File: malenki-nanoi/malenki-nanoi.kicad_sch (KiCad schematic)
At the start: 23 parts, among them J1 Conn_01x02_Male, J2 Conn_01x03, J3 Conn_01x02, J5 Conn_01x02_Male, J6 Conn_01x02_Male, J7 Conn_01x02_Male, U2 AIC1734-33GUTR, U3 ATtiny1616-M, U5 DRV8837DSGR, U6 DRV8837DSGR, U7 DRV8837DSGR

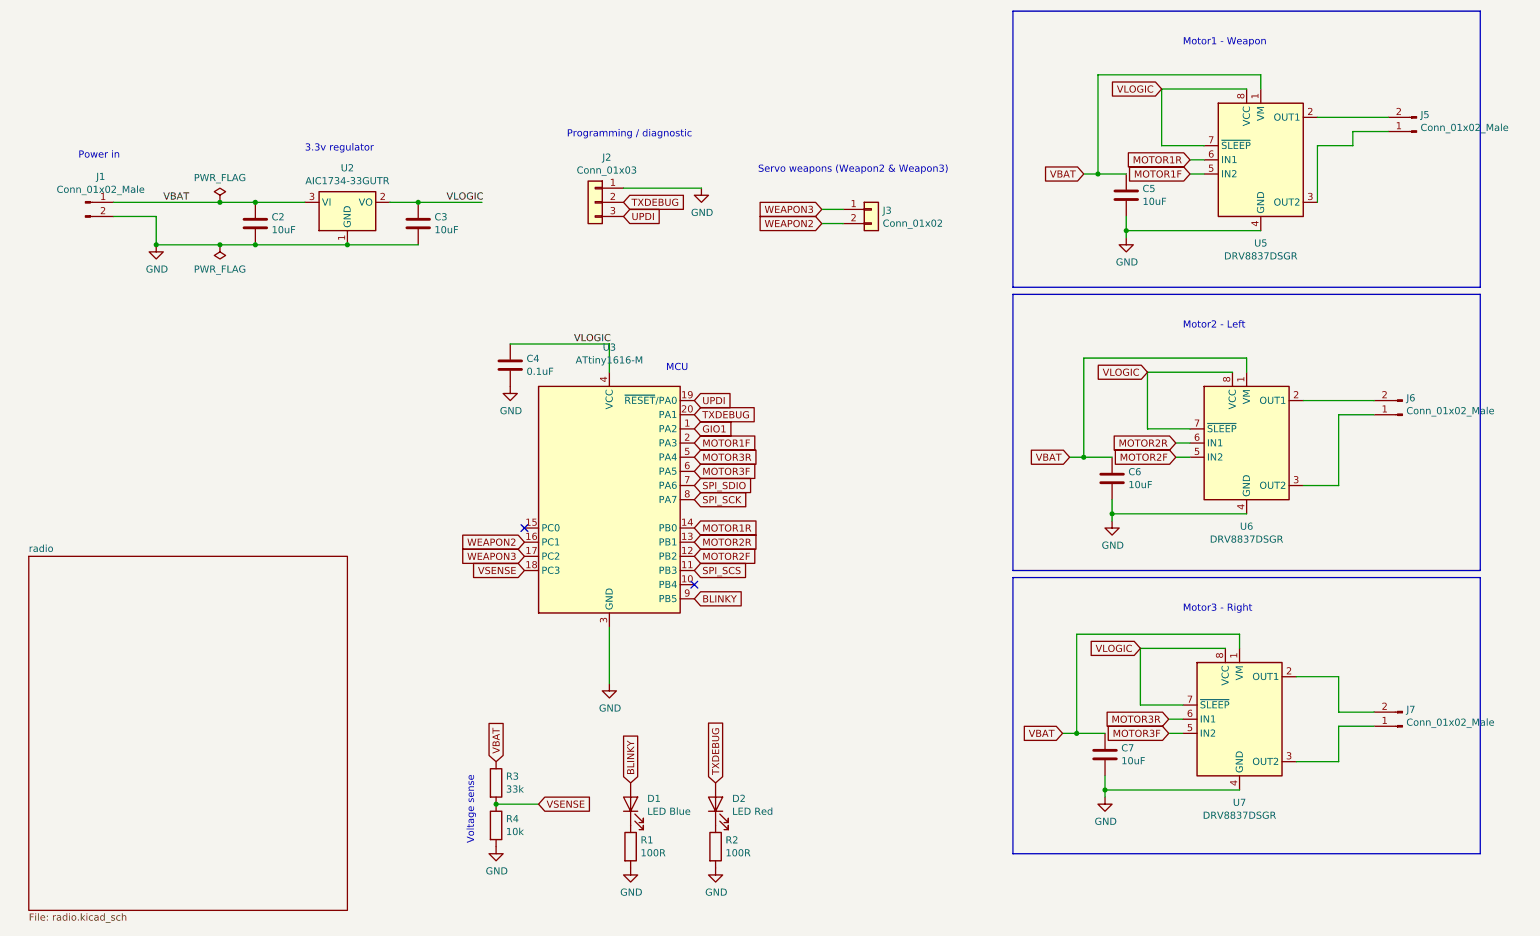
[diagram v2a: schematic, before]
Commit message: 4-layer Malenki-nano
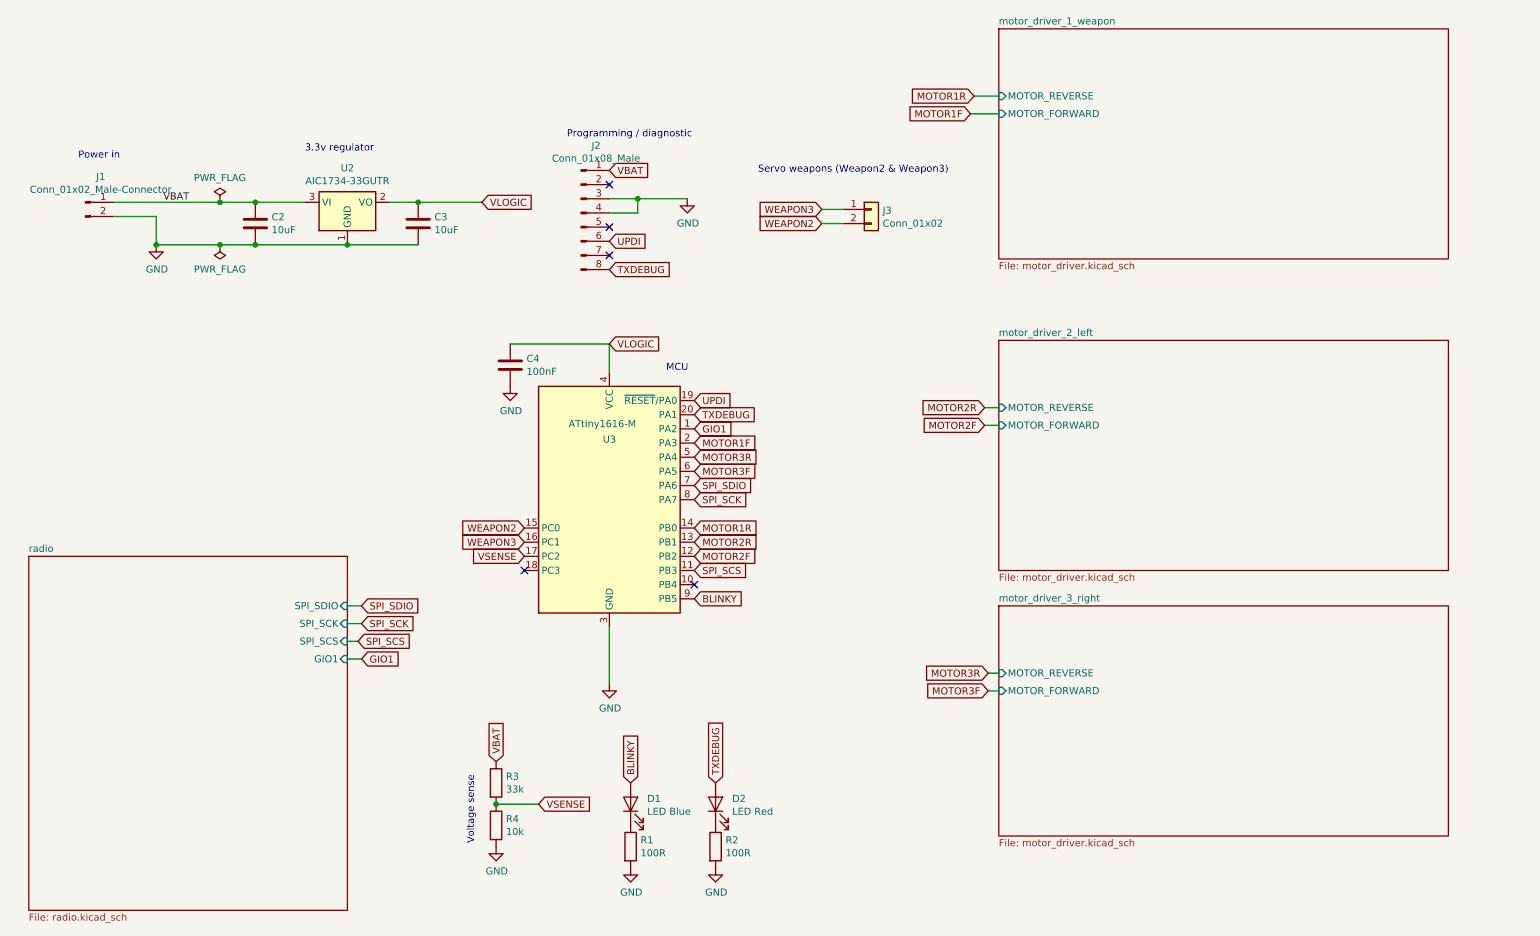
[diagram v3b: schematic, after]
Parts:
- removed C5, C6, C7: 10uF, Capacitor_SMD:C_0603_1608Metric, symbol malenki-nano-rescue:C-Device
- removed J2: Conn_01x03, Connector_PinHeader_2.00mm:PinHeader_1x03_P2.00mm_Vertical, symbol Connector_Generic:Conn_01x03
- removed J5, J6, J7: Conn_01x02_Male, malenki-nano:PinHeader_1x02_P2.54mm_BIG1, symbol malenki-nano-rescue:Conn_01x02_Male-Connector
- removed U5, U6, U7: DRV8837DSGR, malenki-nano:WSON-8-1EP_2x2mm_P0.5mm_HAND1, symbol Driver_Motor:DRV8837C
- added J2: Conn_01x08_Male, malenki-nano:SOIC_clipProgSmall, symbol Connector:Conn_01x08_Male
- C2, C3: LCSC C19702 -> (none)
- C4: value 0.1uF -> 100nF; footprint Capacitor_SMD:C_0603_1608Metric -> Capacitor_SMD:C_0402_1005Metric; LCSC C14663 -> (none)
- D1, D2: footprint LED_SMD:LED_0603_1608Metric_Castellated -> LED_SMD:LED_0603_1608Metric
- J1: value Conn_01x02_Male -> Conn_01x02_Male-Connector
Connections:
- net GND: now also J2.3 (Pin_3), J2.4 (Pin_4)
- net TXDEBUG: now also J2.8 (Pin_8)
- net UPDI: now also J2.6 (Pin_6)
- net VBAT: now also J2.1 (Pin_1)
- net VSENSE: now also U3.17 (PC2); no longer U3.18 (PC3)
- net WEAPON2: now also U3.15 (PC0); no longer U3.16 (PC1)
- net WEAPON3: now also U3.16 (PC1); no longer U3.17 (PC2)
- no-connect marks 2 -> 5
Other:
- added sheet motor_driver_1_weapon (motor_driver.kicad_sch)
- added sheet motor_driver_2_left (motor_driver.kicad_sch)
- added sheet motor_driver_3_right (motor_driver.kicad_sch)
- sheet radio ports: added GIO1, SPI_SCK, SPI_SCS, SPI_SDIO; removed none
- note removed: "Motor1 - Weapon"
- note removed: "Motor2 - Left"
- note removed: "Motor3 - Right"

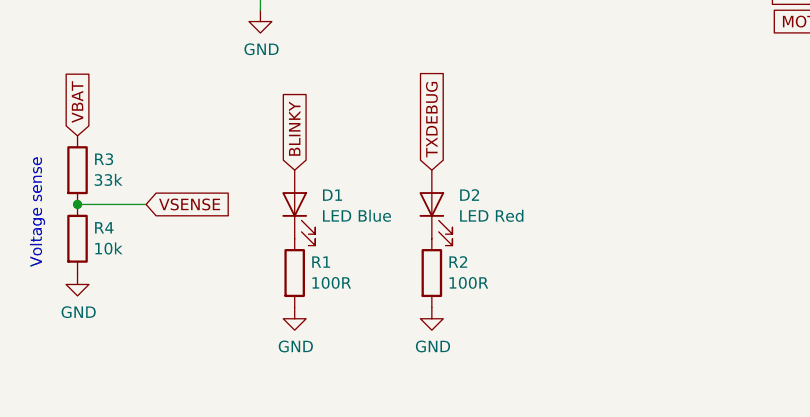
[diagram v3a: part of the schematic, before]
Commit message: Crystal caps update
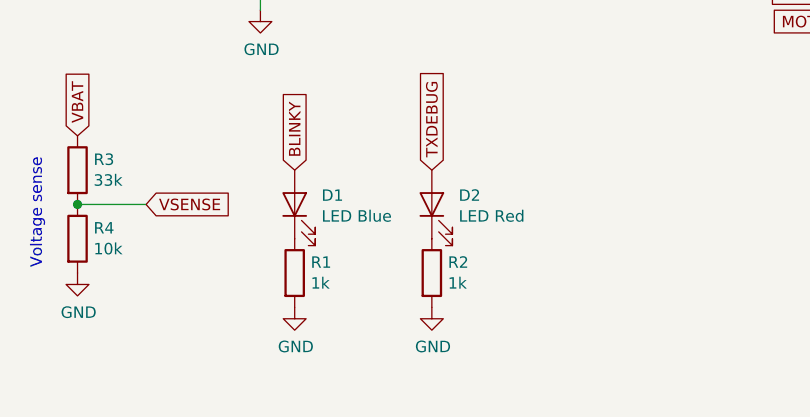
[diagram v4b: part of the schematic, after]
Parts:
- R1, R2: value 100R -> 1k; LCSC C22775 -> (none)
- R3: LCSC C4216 -> (none)
- R4: LCSC C25804 -> (none)
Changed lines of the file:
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@@
   (junction (at 106.68 156.21) (diameter 1.016) (color 0 0 0 0))
   (junction (at 132.08 47.625) (diameter 1.016) (color 0 0 0 0))
+  (no_connect (at 127 57.785))
+  (no_connect (at 142.24 116.84))
+  (no_connect (at 127 52.705))
+  (no_connect (at 111.76 114.3))
   (no_connect (at 127 45.085))
-  (no_connect (at 111.76 114.3))
-  (no_connect (at 142.24 116.84))
-  (no_connect (at 127 57.785))
-  (no_connect (at 127 52.705))
   (wire (pts (xy 38.1 48.26) (xy 57.15 48.26))
     (stroke (width 0) (type solid) (color 0 0 0 0))
@@
       (effects (font (size 1.27 1.27)) hide)
     )
-    (property "LCSC" "C4216" (id 5) (at 106.68 152.4 0)
+    (property "LCSC" "" (id 5) (at 106.68 152.4 0)
       (effects (font (size 1.27 1.27)) hide)
     )
@@
       (effects (font (size 1.27 1.27)) hide)
     )
-    (property "LCSC" "C25804" (id 5) (at 106.68 160.02 0)
+    (property "LCSC" "" (id 5) (at 106.68 160.02 0)
       (effects (font (size 1.27 1.27)) hide)
     )
@@
       (effects (font (size 1.27 1.27)) (justify left))
     )
-    (property "Value" "100R" (id 1) (at 132.588 164.973 0)
+    (property "Value" "1k" (id 1) (at 132.588 164.973 0)
       (effects (font (size 1.27 1.27)) (justify left))
     )
@@
       (effects (font (size 1.27 1.27)) hide)
     )
-    (property "LCSC" "C22775" (id 5) (at 130.81 163.83 0)
+    (property "LCSC" "" (id 5) (at 130.81 163.83 0)
       (effects (font (size 1.27 1.27)) hide)
     )
@@
       (effects (font (size 1.27 1.27)) (justify left))
     )
-    (property "Value" "100R" (id 1) (at 147.828 164.973 0)
+    (property "Value" "1k" (id 1) (at 147.828 164.973 0)
       (effects (font (size 1.27 1.27)) (justify left))
     )
@@
       (effects (font (size 1.27 1.27)) hide)
     )
-    (property "LCSC" "C22775" (id 5) (at 146.05 163.83 0)
+    (property "LCSC" "" (id 5) (at 146.05 163.83 0)
       (effects (font (size 1.27 1.27)) hide)
     )
@@
     )
     (path "/f11a69ac-2dce-40ba-8e3e-2f36b56ed9c7"
-      (reference "R1") (unit 1) (value "100R") (footprint "Resistor_SMD:R_0603_1608Metric")
+      (reference "R1") (unit 1) (value "1k") (footprint "Resistor_SMD:R_0603_1608Metric")
     )
     (path "/29ed0b48-8134-4efe-ba29-799f5df4563b"
-      (reference "R2") (unit 1) (value "100R") (footprint "Resistor_SMD:R_0603_1608Metric")
+      (reference "R2") (unit 1) (value "1k") (footprint "Resistor_SMD:R_0603_1608Metric")
     )
     (path "/9f9c8013-6ba2-4b1f-817e-7aeb8f9ad091"
@@
     )
     (path "/f8865f8d-c9c7-4324-8715-db444b940a42/215e83d2-e873-4735-b43d-b93e560e3c41"
-      (reference "C14") (unit 1) (value "33pF") (footprint "Capacitor_SMD:C_0402_1005Metric")
+      (reference "C14") (unit 1) (value "22pF") (footprint "Capacitor_SMD:C_0402_1005Metric")
     )
     (path "/f8865f8d-c9c7-4324-8715-db444b940a42/089b699b-7234-4ca1-8596-c8152df860db"
-      (reference "C15") (unit 1) (value "33pF") (footprint "Capacitor_SMD:C_0402_1005Metric")
+      (reference "C15") (unit 1) (value "22pF") (footprint "Capacitor_SMD:C_0402_1005Metric")
     )
     (path "/f8865f8d-c9c7-4324-8715-db444b940a42/d104f9b6-35d9-40fd-8206-1975fac53040"

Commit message: Use hand-solder footprints for all 0402
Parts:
- C4: footprint Capacitor_SMD:C_0402_1005Metric -> Capacitor_SMD:C_0402_1005Metric_Pad0.74x0.62mm_HandSolder
- J1, J2: now left out of the parts list
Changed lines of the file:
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@@
   (junction (at 106.68 156.21) (diameter 1.016) (color 0 0 0 0))
   (junction (at 132.08 47.625) (diameter 1.016) (color 0 0 0 0))
+  (no_connect (at 111.76 114.3))
+  (no_connect (at 127 52.705))
   (no_connect (at 127 57.785))
+  (no_connect (at 127 45.085))
   (no_connect (at 142.24 116.84))
-  (no_connect (at 127 52.705))
-  (no_connect (at 111.76 114.3))
-  (no_connect (at 127 45.085))
   (wire (pts (xy 38.1 48.26) (xy 57.15 48.26))
     (stroke (width 0) (type solid) (color 0 0 0 0))
@@
   )
   (symbol (lib_id "malenki-nano-rescue:Conn_01x02_Male-Connector") (at 33.02 48.26 0) (unit 1)
-    (in_bom yes) (on_board yes)
+    (in_bom no) (on_board yes)
     (property "Reference" "J1" (id 0) (at 35.7632 43.6626 0))
     (property "Value" "Conn_01x02_Male-Connector" (id 1) (at 35.7632 45.974 0))
@@
       (effects (font (size 1.27 1.27)) (justify left))
     )
-    (property "Footprint" "Capacitor_SMD:C_0402_1005Metric" (id 2) (at 110.1852 81.28 0)
+    (property "Footprint" "Capacitor_SMD:C_0402_1005Metric_Pad0.74x0.62mm_HandSolder" (id 2) (at 110.1852 81.28 0)
       (effects (font (size 1.27 1.27)) hide)
     )
@@
   )
   (symbol (lib_id "Connector:Conn_01x08_Male") (at 121.92 50.165 0) (unit 1)
-    (in_bom yes) (on_board yes)
+    (in_bom no) (on_board yes)
     (property "Reference" "J2" (id 0) (at 124.6124 38.0808 0))
     (property "Value" "Conn_01x08_Male" (id 1) (at 124.6124 40.3795 0))
@@
     )
     (path "/743e3bfd-2846-452f-87cb-c439c582f82c"
-      (reference "C4") (unit 1) (value "100nF") (footprint "Capacitor_SMD:C_0402_1005Metric")
+      (reference "C4") (unit 1) (value "100nF") (footprint "Capacitor_SMD:C_0402_1005Metric_Pad0.74x0.62mm_HandSolder")
     )
     (path "/873f0869-df80-4fe6-817c-973a36517086"
@@
     )
     (path "/f8865f8d-c9c7-4324-8715-db444b940a42/66cb42e5-4d9e-40a2-a2c4-9364eaae7141"
-      (reference "C9") (unit 1) (value "1pF") (footprint "Capacitor_SMD:C_0402_1005Metric")
+      (reference "C9") (unit 1) (value "1pF") (footprint "Capacitor_SMD:C_0402_1005Metric_Pad0.74x0.62mm_HandSolder")
     )
     (path "/f8865f8d-c9c7-4324-8715-db444b940a42/19f9ce3e-6112-47c3-be9c-52edb46d1400"
-      (reference "C10") (unit 1) (value "22pF") (footprint "Capacitor_SMD:C_0402_1005Metric")
+      (reference "C10") (unit 1) (value "22pF") (footprint "Capacitor_SMD:C_0402_1005Metric_Pad0.74x0.62mm_HandSolder")
     )
     (path "/f8865f8d-c9c7-4324-8715-db444b940a42/19c72677-c166-4d54-8f59-572a153580c0"
-      (reference "C11") (unit 1) (value "10pF") (footprint "Capacitor_SMD:C_0402_1005Metric")
+      (reference "C11") (unit 1) (value "10pF") (footprint "Capacitor_SMD:C_0402_1005Metric_Pad0.74x0.62mm_HandSolder")
     )
     (path "/f8865f8d-c9c7-4324-8715-db444b940a42/0b0030e3-97d6-4726-b917-72c61fef63d8"
-      (reference "C12") (unit 1) (value "100nF") (footprint "Capacitor_SMD:C_0402_1005Metric")
+      (reference "C12") (unit 1) (value "100nF") (footprint "Capacitor_SMD:C_0402_1005Metric_Pad0.74x0.62mm_HandSolder")
     )
     (path "/f8865f8d-c9c7-4324-8715-db444b940a42/f33e7671-b9c8-40c2-9120-c03d59cd8f50"
-      (reference "C13") (unit 1) (value "100nF") (footprint "Capacitor_SMD:C_0402_1005Metric")
+      (reference "C13") (unit 1) (value "100nF") (footprint "Capacitor_SMD:C_0402_1005Metric_Pad0.74x0.62mm_HandSolder")
     )
     (path "/f8865f8d-c9c7-4324-8715-db444b940a42/215e83d2-e873-4735-b43d-b93e560e3c41"
-      (reference "C14") (unit 1) (value "22pF") (footprint "Capacitor_SMD:C_0402_1005Metric")
+      (reference "C14") (unit 1) (value "22pF") (footprint "Capacitor_SMD:C_0402_1005Metric_Pad0.74x0.62mm_HandSolder")
     )
     (path "/f8865f8d-c9c7-4324-8715-db444b940a42/089b699b-7234-4ca1-8596-c8152df860db"
-      (reference "C15") (unit 1) (value "22pF") (footprint "Capacitor_SMD:C_0402_1005Metric")
+      (reference "C15") (unit 1) (value "22pF") (footprint "Capacitor_SMD:C_0402_1005Metric_Pad0.74x0.62mm_HandSolder")
     )
     (path "/f8865f8d-c9c7-4324-8715-db444b940a42/d104f9b6-35d9-40fd-8206-1975fac53040"
-      (reference "C16") (unit 1) (value "100nF") (footprint "Capacitor_SMD:C_0402_1005Metric")
+      (reference "C16") (unit 1) (value "100nF") (footprint "Capacitor_SMD:C_0402_1005Metric_Pad0.74x0.62mm_HandSolder")
     )
     (path "/f8865f8d-c9c7-4324-8715-db444b940a42/ed3b10e6-1f62-4694-a165-a81089d52184"
-      (reference "C17") (unit 1) (value "100nF") (footprint "Capacitor_SMD:C_0402_1005Metric")
+      (reference "C17") (unit 1) (value "100nF") (footprint "Capacitor_SMD:C_0402_1005Metric_Pad0.74x0.62mm_HandSolder")
     )
     (path "/f8865f8d-c9c7-4324-8715-db444b940a42/dfcc0291-fde2-4968-8dfe-dc0fed520275"
-      (reference "C18") (unit 1) (value "560pF") (footprint "Capacitor_SMD:C_0402_1005Metric")
+      (reference "C18") (unit 1) (value "560pF") (footprint "Capacitor_SMD:C_0402_1005Metric_Pad0.74x0.62mm_HandSolder")
     )
     (path "/f8865f8d-c9c7-4324-8715-db444b940a42/61da5400-349c-4f48-a162-f52487e1921d"
-      (reference "C19") (unit 1) (value "10nF") (footprint "Capacitor_SMD:C_0402_1005Metric")
+      (reference "C19") (unit 1) (value "10nF") (footprint "Capacitor_SMD:C_0402_1005Metric_Pad0.74x0.62mm_HandSolder")
     )
     (path "/f8865f8d-c9c7-4324-8715-db444b940a42/6545753d-6d1e-4127-b61a-3db1ceec6d42"
@@
     )
     (path "/f8865f8d-c9c7-4324-8715-db444b940a42/52e761a0-c28e-41e0-a3bd-b32a8696a976"
-      (reference "C22") (unit 1) (value "100nF") (footprint "Capacitor_SMD:C_0402_1005Metric")
+      (reference "C22") (unit 1) (value "100nF") (footprint "Capacitor_SMD:C_0402_1005Metric_Pad0.74x0.62mm_HandSolder")
     )
     (path "/f8865f8d-c9c7-4324-8715-db444b940a42/f65ffae7-fc80-4563-89b6-6365862c5faa"
-      (reference "C23") (unit 1) (value "100nF") (footprint "Capacitor_SMD:C_0402_1005Metric")
+      (reference "C23") (unit 1) (value "100nF") (footprint "Capacitor_SMD:C_0402_1005Metric_Pad0.74x0.62mm_HandSolder")
     )
     (path "/f8865f8d-c9c7-4324-8715-db444b940a42/d45315c2-46f0-47a6-b716-e74dc67406db"
-      (reference "L1") (unit 1) (value "2.7nH") (footprint "Inductor_SMD:L_0402_1005Metric")
+      (reference "L1") (unit 1) (value "2.7nH") (footprint "Inductor_SMD:L_0402_1005Metric_Pad0.77x0.64mm_HandSolder")
     )
     (path "/f8865f8d-c9c7-4324-8715-db444b940a42/580c6d2b-a8e3-498e-8012-27d587656f3b"
-      (reference "L2") (unit 1) (value "4.7nH") (footprint "Inductor_SMD:L_0402_1005Metric")
+      (reference "L2") (unit 1) (value "4.7nH") (footprint "Inductor_SMD:L_0402_1005Metric_Pad0.77x0.64mm_HandSolder")
     )
     (path "/f8865f8d-c9c7-4324-8715-db444b940a42/c420d0bf-bb38-4822-8699-2971a00ad3de"
-      (reference "L3") (unit 1) (value "4.7nH") (footprint "Inductor_SMD:L_0402_1005Metric")
+      (reference "L3") (unit 1) (value "4.7nH") (footprint "Inductor_SMD:L_0402_1005Metric_Pad0.77x0.64mm_HandSolder")
     )
     (path "/f8865f8d-c9c7-4324-8715-db444b940a42/5902e9a6-0dad-47d3-b107-e5e2b73c9336"
-      (reference "R5") (unit 1) (value "200R") (footprint "Resistor_SMD:R_0402_1005Metric")
+      (reference "R5") (unit 1) (value "200R") (footprint "Resistor_SMD:R_0402_1005Metric_Pad0.72x0.64mm_HandSolder")
     )
     (path "/f8865f8d-c9c7-4324-8715-db444b940a42/521b88df-0024-429c-a691-655a8edd80c0"
